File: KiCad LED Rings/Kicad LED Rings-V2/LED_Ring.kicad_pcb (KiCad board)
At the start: 4 copper layers, 30 x 30 mm, 28 parts, among them J1 Conn_01x02_Female, J2 Conn_01x02_Male, U1 LM3509SD_NOPB

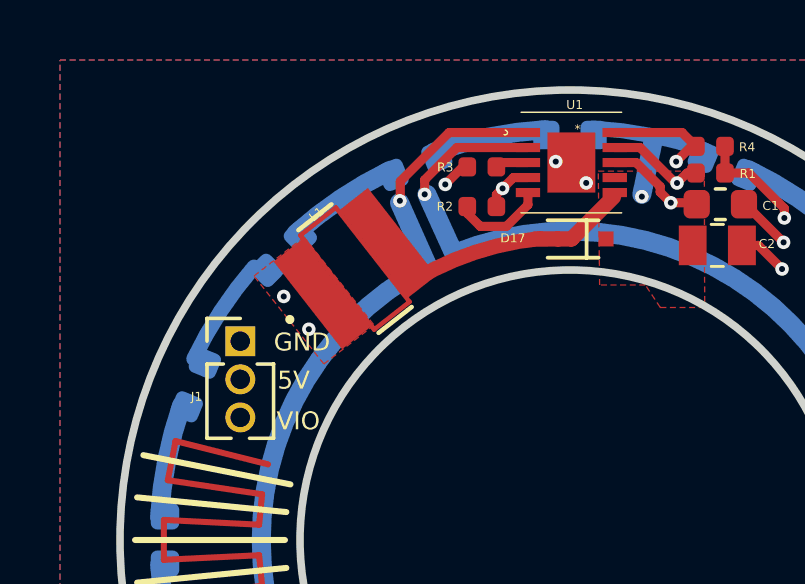
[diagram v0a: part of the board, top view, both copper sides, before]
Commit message: updated led ring pcb board
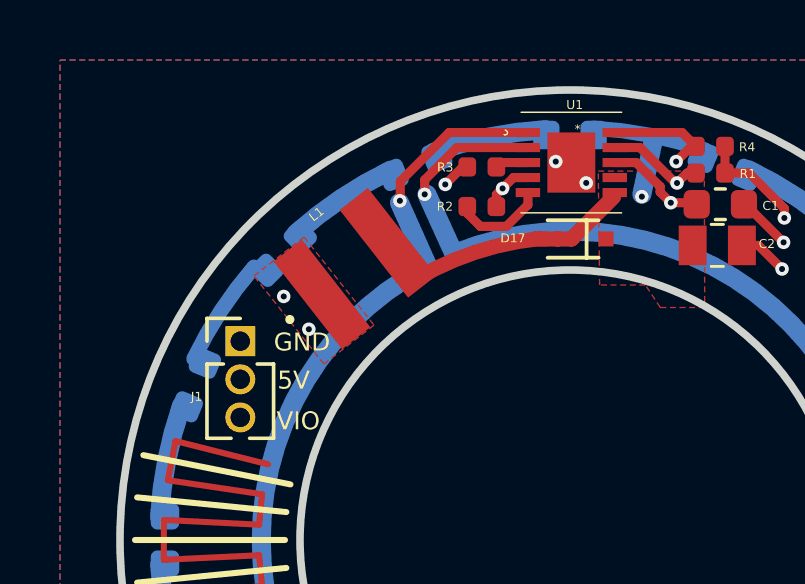
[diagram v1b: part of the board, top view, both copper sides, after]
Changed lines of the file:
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@@
-(kicad_pcb (version 20171130) (host pcbnew "(5.1.6)-1")
+(kicad_pcb (version 20171130) (host pcbnew "(5.1.4)-1")
   (general
     (thickness 1.6)
@@
       (drillshape 0)
       (scaleselection 1)
-      (outputdirectory "Output/"))
+      (outputdirectory "Gerber/"))
   )
   (net 0 "")
@@
     (add_net SCL)
     (add_net SDA)
+  )
+  (module footprints:NRS4012T100MDGJ (layer F.Cu)
+    (at 102.833095 70.952848 38)
+    (attr smd)
+    (fp_text reference L1 (at 0.105116 -2.219934 38) (layer F.SilkS)
+      (effects (font (size 0.3 0.3) (thickness 0.05)))
+    )
+    (fp_text value 10uH (at 0 0 38) (layer F.SilkS) hide
+      (effects (font (size 1 1) (thickness 0.15)))
+    )
+    (fp_line (start -2.0447 2.0447) (end 2.0447 2.0447) (layer F.Fab) (width 0.1524))
+    (fp_line (start 2.0447 2.0447) (end 2.0447 -2.0447) (layer F.Fab) (width 0.1524))
+    (fp_line (start 2.0447 -2.0447) (end -2.0447 -2.0447) (layer F.Fab) (width 0.1524))
+    (fp_line (start -2.0447 -2.0447) (end -2.0447 2.0447) (layer F.Fab) (width 0.1524))
+    (fp_line (start -2.2987 2.1082) (end -2.2987 -2.1082) (layer F.CrtYd) (width 0.1524))
+    (fp_line (start -2.2987 -2.1082) (end -2.2987 -2.1082) (layer F.CrtYd) (width 0.1524))
+    (fp_line (start -2.2987 -2.1082) (end -2.2987 -2.2987) (layer F.CrtYd) (width 0.1524))
+    (fp_line (start -2.2987 -2.2987) (end 2.2987 -2.2987) (layer F.CrtYd) (width 0.1524))
+    (fp_line (start 2.2987 -2.2987) (end 2.2987 -2.1082) (layer F.CrtYd) (width 0.1524))
+    (fp_line (start 2.2987 -2.1082) (end 2.2987 -2.1082) (layer F.CrtYd) (width 0.1524))
+    (fp_line (start 2.2987 -2.1082) (end 2.2987 2.1082) (layer F.CrtYd) (width 0.1524))
+    (fp_line (start 2.2987 2.1082) (end 2.2987 2.1082) (layer F.CrtYd) (width 0.1524))
+    (fp_line (start 2.2987 2.1082) (end 2.2987 2.2987) (layer F.CrtYd) (width 0.1524))
+    (fp_line (start 2.2987 2.2987) (end -2.2987 2.2987) (layer F.CrtYd) (width 0.1524))
+    (fp_line (start -2.2987 2.2987) (end -2.2987 2.1082) (layer F.CrtYd) (width 0.1524))
+    (fp_line (start -2.2987 2.1082) (end -2.2987 2.1082) (layer F.CrtYd) (width 0.1524))
+    (fp_circle (center -1.9685 0) (end -1.8923 0) (layer F.Fab) (width 0.1524))
+    (fp_circle (center -2.7559 0) (end -2.6797 0) (layer F.SilkS) (width 0.1524))
+    (fp_text user "Copyright 2016 Accelerated Designs. All rights reserved." (at 0 0 38) (layer Cmts.User)
+      (effects (font (size 0.127 0.127) (thickness 0.002)))
+    )
+    (fp_text user * (at 0 0 38) (layer F.SilkS) hide
+      (effects (font (size 1 1) (thickness 0.15)))
+    )
+    (fp_text user * (at 0 0 38) (layer F.Fab)
+      (effects (font (size 1 1) (thickness 0.15)))
+    )
+    (fp_text user 0.146in/3.708mm (at 4.9022 0 38) (layer Dwgs.User)
+      (effects (font (size 1 1) (thickness 0.15)))
+    )
+    (fp_text user 0.157in/3.988mm (at 0 5.0927 38) (layer Dwgs.User)
+      (effects (font (size 1 1) (thickness 0.15)))
+    )
+    (fp_text user 0.063in/1.6mm (at 0 -5.0927 38) (layer Dwgs.User)
+      (effects (font (size 1 1) (thickness 0.15)))
+    )
+    (pad 1 smd rect (at -1.397 0 38) (size 1.1938 3.7084) (layers F.Cu F.Paste F.Mask)
+      (net 1 +5V))
+    (pad 2 smd rect (at 1.397 0 38) (size 1.1938 3.7084) (layers F.Cu F.Paste F.Mask)
+      (net 25 "Net-(D17-Pad2)"))
+    (model "L:/Behavior Camera/KiCad LED Rings/10uH Inductor/NRS4012T100MDGJ/ul_NRS4012T100MDGJ/STEP/IND_TAIYO_NRS4012_TAY.step"
+      (at (xyz 0 0 0))
+      (scale (xyz 1 1 1))
+      (rotate (xyz 0 0 0))
+    )
   )
   (module .Logo:Minicam_LED_Ring (layer B.Cu)
@@
     )
   )
-  (module footprints:NRS4012T100MDGJ (layer F.Cu)
-    (at 102.833095 70.952848 38)
-    (attr smd)
-    (fp_text reference L1 (at 0.105116 -2.219934 38) (layer F.SilkS)
-      (effects (font (size 0.3 0.3) (thickness 0.05)))
-    )
-    (fp_text value 10uH (at 0 0 38) (layer F.SilkS) hide
-      (effects (font (size 1 1) (thickness 0.15)))
-    )
-    (fp_line (start -0.700553 2.1717) (end 0.700553 2.1717) (layer F.SilkS) (width 0.1524))
-    (fp_line (start 0.700553 -2.1717) (end -0.700553 -2.1717) (layer F.SilkS) (width 0.1524))
-    (fp_line (start -2.0447 2.0447) (end 2.0447 2.0447) (layer F.Fab) (width 0.1524))
-    (fp_line (start 2.0447 2.0447) (end 2.0447 -2.0447) (layer F.Fab) (width 0.1524))
-    (fp_line (start 2.0447 -2.0447) (end -2.0447 -2.0447) (layer F.Fab) (width 0.1524))
-    (fp_line (start -2.0447 -2.0447) (end -2.0447 2.0447) (layer F.Fab) (width 0.1524))
-    (fp_line (start -0.7493 -1.9939) (end 0.7493 -1.9939) (layer F.Cu) (width 0.1524))
-    (fp_line (start 0.7493 -1.9939) (end 0.7493 1.9939) (layer F.Cu) (width 0.1524))
-    (fp_line (start 0.7493 1.9939) (end -0.7493 1.9939) (layer F.Cu) (width 0.1524))
-    (fp_line (start -0.7493 1.9939) (end -0.7493 -1.9939) (layer F.Cu) (width 0.1524))
-    (fp_line (start -2.2987 2.1082) (end -2.2987 -2.1082) (layer F.CrtYd) (width 0.1524))
-    (fp_line (start -2.2987 -2.1082) (end -2.2987 -2.1082) (layer F.CrtYd) (width 0.1524))
-    (fp_line (start -2.2987 -2.1082) (end -2.2987 -2.2987) (layer F.CrtYd) (width 0.1524))
-    (fp_line (start -2.2987 -2.2987) (end 2.2987 -2.2987) (layer F.CrtYd) (width 0.1524))
-    (fp_line (start 2.2987 -2.2987) (end 2.2987 -2.1082) (layer F.CrtYd) (width 0.1524))
-    (fp_line (start 2.2987 -2.1082) (end 2.2987 -2.1082) (layer F.CrtYd) (width 0.1524))
-    (fp_line (start 2.2987 -2.1082) (end 2.2987 2.1082) (layer F.CrtYd) (width 0.1524))
-    (fp_line (start 2.2987 2.1082) (end 2.2987 2.1082) (layer F.CrtYd) (width 0.1524))
-    (fp_line (start 2.2987 2.1082) (end 2.2987 2.2987) (layer F.CrtYd) (width 0.1524))
-    (fp_line (start 2.2987 2.2987) (end -2.2987 2.2987) (layer F.CrtYd) (width 0.1524))
-    (fp_line (start -2.2987 2.2987) (end -2.2987 2.1082) (layer F.CrtYd) (width 0.1524))
-    (fp_line (start -2.2987 2.1082) (end -2.2987 2.1082) (layer F.CrtYd) (width 0.1524))
-    (fp_circle (center -1.9685 0) (end -1.8923 0) (layer F.Fab) (width 0.1524))
-    (fp_circle (center -2.7559 0) (end -2.6797 0) (layer F.SilkS) (width 0.1524))
-    (fp_text user "Copyright 2016 Accelerated Designs. All rights reserved." (at 0 0 38) (layer Cmts.User)
-      (effects (font (size 0.127 0.127) (thickness 0.002)))
-    )
-    (fp_text user * (at 0 0 38) (layer F.SilkS) hide
-      (effects (font (size 1 1) (thickness 0.15)))
-    )
-    (fp_text user * (at 0 0 38) (layer F.Fab)
-      (effects (font (size 1 1) (thickness 0.15)))
-    )
-    (fp_text user 0.146in/3.708mm (at 4.9022 0 38) (layer Dwgs.User)
-      (effects (font (size 1 1) (thickness 0.15)))
-    )
-    (fp_text user 0.157in/3.988mm (at 0 5.0927 38) (layer Dwgs.User)
-      (effects (font (size 1 1) (thickness 0.15)))
-    )
-    (fp_text user 0.063in/1.6mm (at 0 -5.0927 38) (layer Dwgs.User)
-      (effects (font (size 1 1) (thickness 0.15)))
-    )
-    (pad 1 smd rect (at -1.397 0 38) (size 1.1938 3.7084) (layers F.Cu F.Paste F.Mask)
-      (net 1 +5V))
-    (pad 2 smd rect (at 1.397 0 38) (size 1.1938 3.7084) (layers F.Cu F.Paste F.Mask)
-      (net 25 "Net-(D17-Pad2)"))
-    (model "L:/Behavior Camera/KiCad LED Rings/10uH Inductor/NRS4012T100MDGJ/ul_NRS4012T100MDGJ/STEP/IND_TAIYO_NRS4012_TAY.step"
-      (at (xyz 0 0 0))
-      (scale (xyz 1 1 1))
-      (rotate (xyz 0 0 0))
-    )
-  )
   (module Resistor_SMD:R_0402_1005Metric (layer F.Cu)
     (at 114.681 67.7672)
@@
       (at (xyz 0 0 0))
       (scale (xyz 1 1 1))
-      (rotate (xyz 30 0 0))
+      (rotate (xyz -90 0 0))
     )
     (model ${KICAD_AHARONI_LAB}/KiCad-Library-master/Modules/Capacitor.pretty/C_0805_2012Metric_L.STEP
       (at (xyz 0 0 0))
       (scale (xyz 1 1 1))
-      (rotate (xyz -90 0 0))
-    )
-  )
+      (rotate (xyz -15 0 0))
+    )
+  )
